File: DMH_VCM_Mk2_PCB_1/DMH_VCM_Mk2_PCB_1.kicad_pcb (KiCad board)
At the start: 2 copper layers, 48 x 175 mm, 95 parts, among them J1 TS_Jack_6.35mm_Sw, J10 TS_Jack_6.35mm_Sw, J100 IDC_02x05, J2 TS_Jack_6.35mm_Sw, J200 IDC_02x05, J3 TS_Jack_6.35mm_Sw, J4 TS_Jack_6.35mm_Sw, J5 TS_Jack_6.35mm_Sw, J50 Conn_01x08, J6 TS_Jack_6.35mm_Sw, J60 Conn_01x08, J7 TS_Jack_6.35mm_Sw, J70 Conn_01x08, J8 TS_Jack_6.35mm_Sw, J9 TS_Jack_6.35mm_Sw, Q1 BC548, Q2 BC548, Q3 BC548, Q4 BC548, Q5 BC548, Q6 BC548, U1 TL074, U2 TL074, U3 TL074

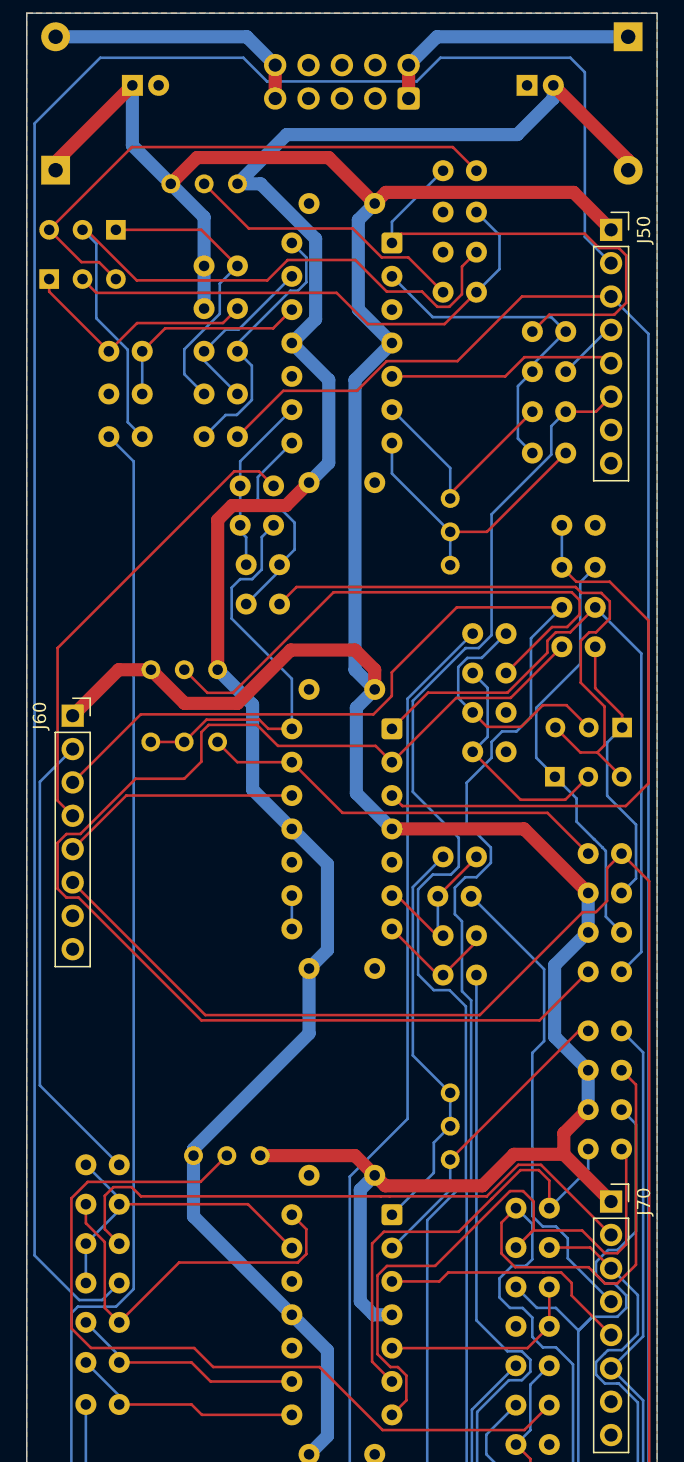
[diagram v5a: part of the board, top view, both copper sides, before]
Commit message: Fixed routing bugs
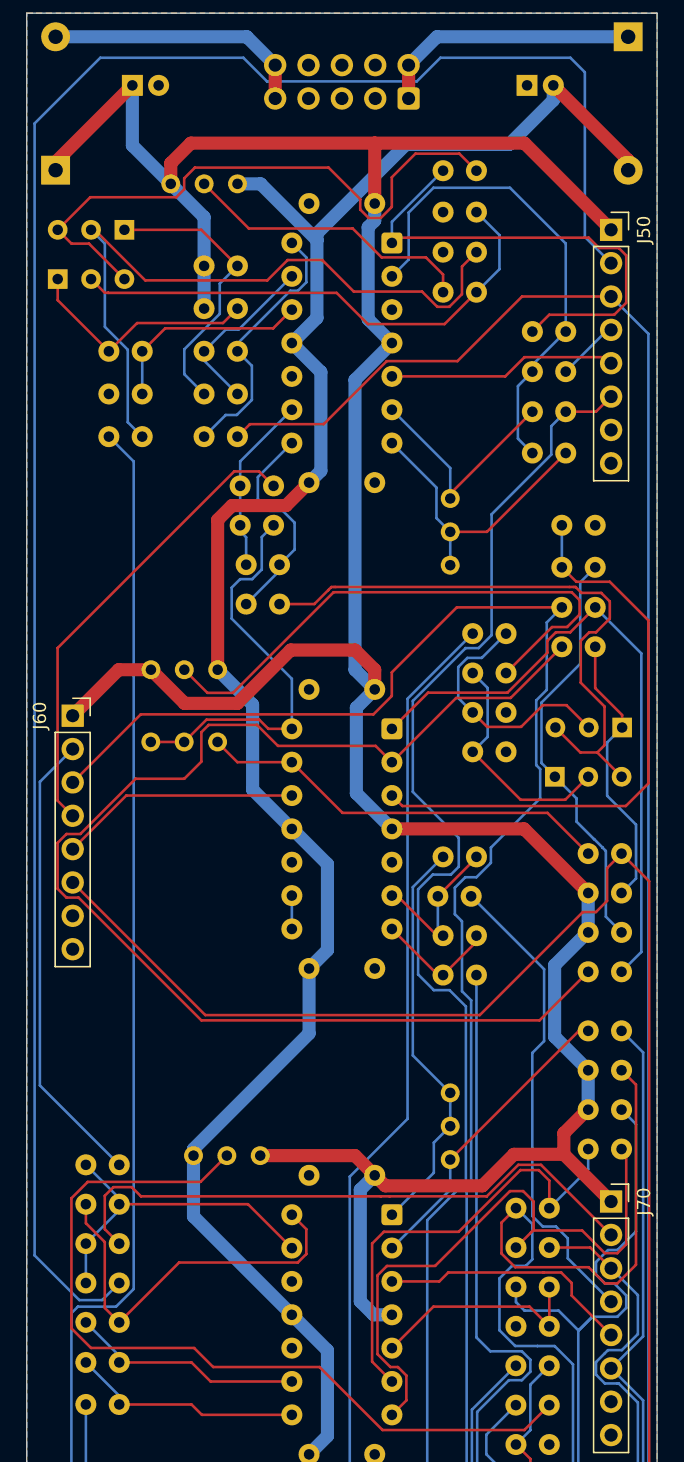
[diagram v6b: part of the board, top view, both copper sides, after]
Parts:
- moved Q1 0.65 mm to (58.4, 59.0)
- moved Q2 0.65 mm to (53.4, 62.8)
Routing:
- net Net-(U1A--): track 26.2 -> 37.8 mm
- net +12V: track 230.3 -> 235.5 mm
- net Net-(Q1-E): track 42.5 -> 46.9 mm
- net -12V: track 157.2 -> 152.8 mm
- net /Inputs and Outputs/Output B Jack: track 151.2 -> 149.3 mm
- net Net-(U3B-+): track 15.7 -> 16.9 mm
- net Net-(Q1-B): track 54.3 -> 53.4 mm
- net Net-(R9-Pad1): track 21.6 -> 22.4 mm
- net Net-(Q5-E): track 57.7 -> 58.5 mm
- net Net-(Q6-C): track 60.4 -> 61.1 mm
- net Net-(Q2-B): track 40.0 -> 39.3 mm
- net Net-(Q1-C): track 22.4 -> 21.8 mm
- net Net-(Q5-C): track 64.5 -> 65.1 mm

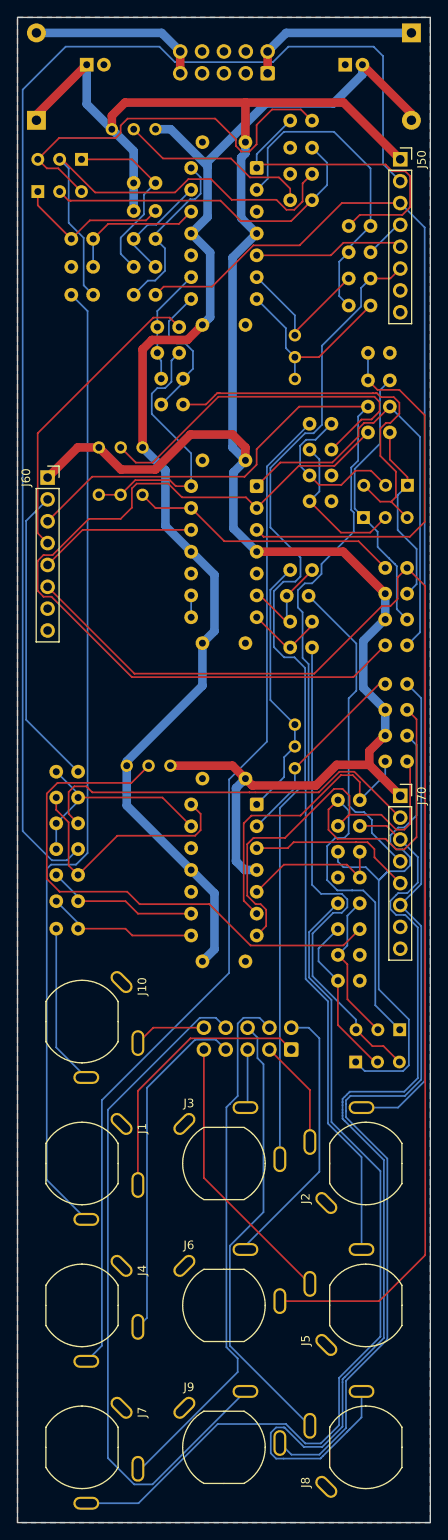
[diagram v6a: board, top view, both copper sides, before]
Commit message: Optimized PCB 1 routing
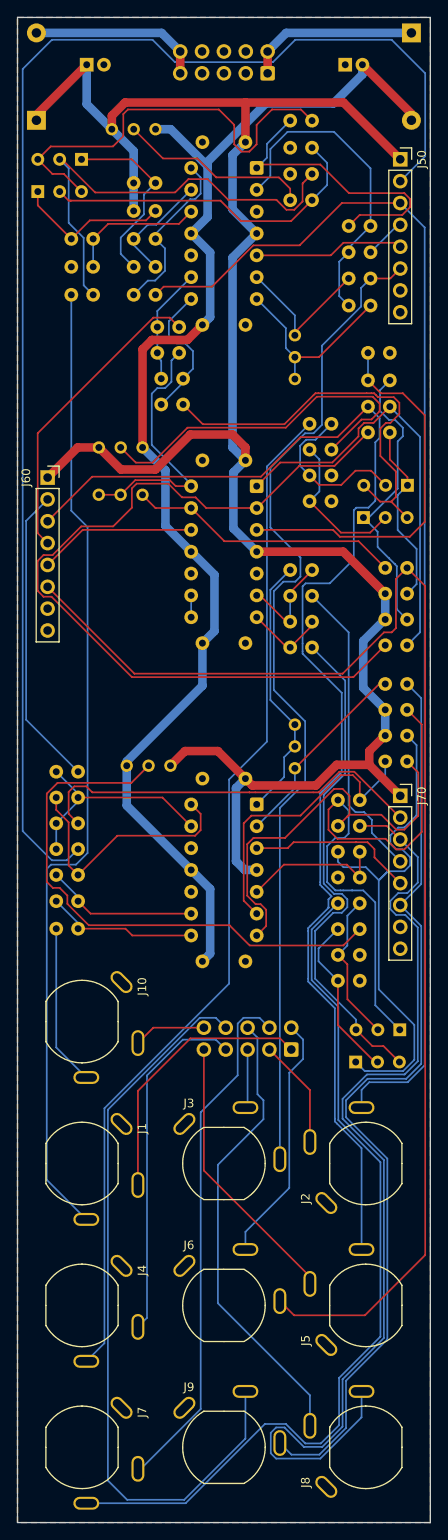
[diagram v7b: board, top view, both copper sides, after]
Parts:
- moved R45 0.40 mm to (85.2, 109.8)
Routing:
- net /Inputs and Outputs/Mute A Switch: track 155.9 -> 162.7 mm
- net Net-(J200-Pin_9): track 80.8 -> 87.1 mm
- net /Inputs and Outputs/Output B Jack: track 149.3 -> 154.7 mm
- net /Inputs and Outputs/CV B Jack: track 152.4 -> 155.7 mm
- net Net-(J200-Pin_6): track 31.9 -> 29.1 mm
- net Net-(Q1-E): track 46.9 -> 49.7 mm
- net +12V: track 235.5 -> 237.7 mm
- net Net-(Q4-C): track 32.0 -> 34.2 mm
- net Net-(Q3-E): track 46.4 -> 48.3 mm
- net Net-(R12-Pad1): track 37.3 -> 35.8 mm
- net Net-(J200-Pin_8): track 52.5 -> 53.7 mm
- net /Inputs and Outputs/Output C Jack: track 118.4 -> 117.2 mm
- net Net-(J200-Pin_7): track 62.3 -> 61.2 mm
- net /Inputs and Outputs/CV C Jack: track 110.1 -> 109.0 mm
- net Net-(Q5-E): track 58.5 -> 59.5 mm
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
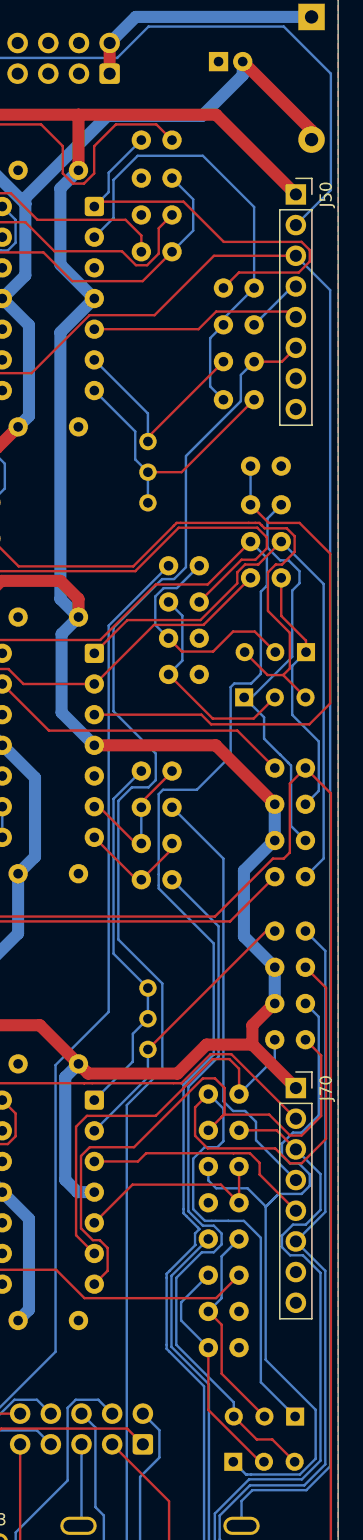
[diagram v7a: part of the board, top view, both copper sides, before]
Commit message: Resolved J50 volume conflict
J70 still to be solved
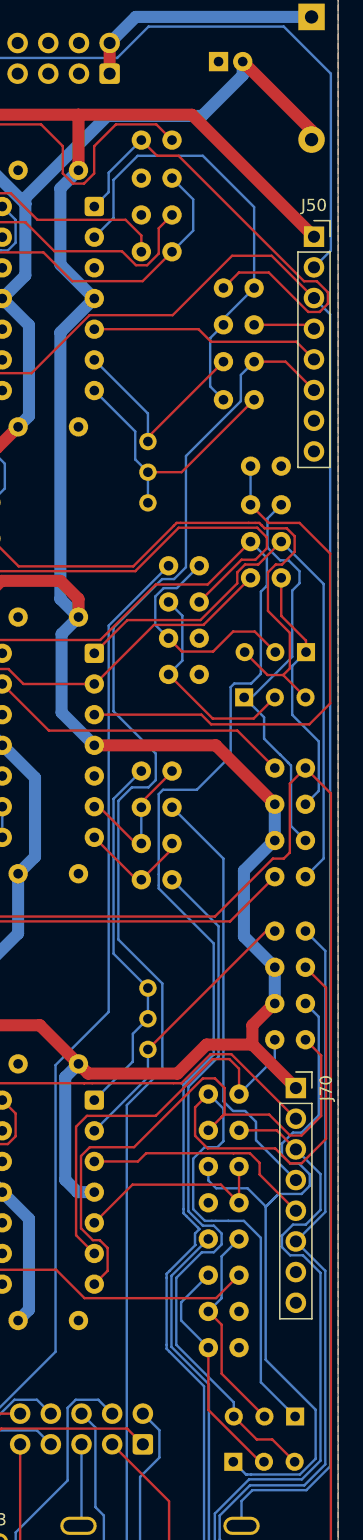
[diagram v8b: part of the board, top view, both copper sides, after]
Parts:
- moved J50 3.81 mm to (97.0, 62.5)
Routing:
- net Net-(R12-Pad1): track 35.8 -> 39.5 mm
- net +12V: track 237.7 -> 240.6 mm
- net /Inputs and Outputs/Mute A Switch: track 162.7 -> 165.6 mm
- net /Inputs and Outputs/CV A Jack: track 118.0 -> 120.0 mm
- net /Inputs and Outputs/CV Amt A Pot: track 17.5 -> 19.2 mm
- net /Inputs and Outputs/Output A Jack: track 144.9 -> 143.7 mm
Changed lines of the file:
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@@
 		(locked yes)
 		(layer "F.Cu")
-		(at 95.5 59)
+		(at 97 62.5)
 		(descr "Through hole straight socket strip, 1x08, 2.54mm pitch, single row (from Kicad 4.0.7), script generated")
 		(tags "Through hole socket strip THT 1x08 2.54mm single row")
 		(property "Reference" "J50"
-			(at 2.5 0 90)
+			(at 0 -2.6 180)
 			(layer "F.SilkS")
 			(effects
@@
 		(tags "Resistor Axial_DIN0207 series Axial Vertical pin pitch 2.54mm 0.25W = 1/4W length 6.3mm diameter 2.5mm")
 		(property "Reference" "R22"
-			(at 5.11 -0.1 0)
+			(at 1.35 -2.1 0)
 			(layer "B.SilkS")
 			(effects
@@
 	)
 	(segment
+		(start 86.9 52.4)
+		(end 97 62.5)
+		(width 1)
+		(layer "F.Cu")
+		(net 1)
+	)
+	(segment
 		(start 78.81 104.62)
 		(end 88.875 104.62)
@@
 	)
 	(segment
-		(start 88.9 52.4)
-		(end 95.5 59)
-		(width 1)
-		(layer "F.Cu")
-		(net 1)
-	)
-	(segment
 		(start 76 91)
 		(end 77.5 92.5)
@@
 	)
 	(segment
-		(start 77.5 52.4)
-		(end 88.9 52.4)
-		(width 1)
-		(layer "F.Cu")
-		(net 1)
-	)
-	(segment
 		(start 63.5 52.4)
 		(end 77.5 52.4)
@@
 	)
 	(segment
+		(start 77.5 52.4)
+		(end 86.9 52.4)
+		(width 1)
+		(layer "F.Cu")
+		(net 1)
+	)
+	(segment
 		(start 76.1 95.4)
 		(end 76.1 101.91)
@@
 	)
 	(segment
+		(start 93.5 64.08)
+		(end 97 67.58)
+		(width 0.2)
+		(layer "F.Cu")
+		(net 9)
+	)
+	(segment
 		(start 67.045 74.75)
 		(end 67.995 73.8)
@@
 	)
 	(segment
-		(start 83.8 69)
-		(end 88.72 64.08)
+		(start 85.3 69)
+		(end 90.22 64.08)
 		(width 0.2)
 		(layer "F.Cu")
@@
 	)
 	(segment
-		(start 88.72 64.08)
-		(end 95.5 64.08)
+		(start 90.22 64.08)
+		(end 93.5 64.08)
 		(width 0.2)
 		(layer "F.Cu")
@@
 	(segment
 		(start 78.41295 69)
-		(end 83.8 69)
+		(end 85.3 69)
 		(width 0.2)
 		(layer "F.Cu")
@@
 	)
 	(segment
-		(start 96.3661 166.301)
-		(end 91.899 166.301)
+		(start 98.341 68.921)
+		(end 98.341 164.3261)
 		(width 0.2)
 		(layer "B.Cu")
@@
 	)
 	(segment
-		(start 95.5 64.08)
-		(end 98.341 66.921)
+		(start 96.3661 166.301)
+		(end 91.899 166.301)
 		(width 0.2)
 		(layer "B.Cu")
@@
 	)
 	(segment
-		(start 91.899 166.301)
-		(end 91 167.2)
+		(start 97 67.58)
+		(end 98.341 68.921)
 		(width 0.2)
 		(layer "B.Cu")
@@
 	)
 	(segment
-		(start 91 167.2)
-		(end 91 169.25)
+		(start 98.341 164.3261)
+		(end 96.3661 166.301)
 		(width 0.2)
 		(layer "B.Cu")
@@
 	)
 	(segment
-		(start 98.341 66.921)
-		(end 98.341 164.3261)
+		(start 91.899 166.301)
+		(end 91 167.2)
 		(width 0.2)
 		(layer "B.Cu")
@@
 	)
 	(segment
-		(start 98.341 164.3261)
-		(end 96.3661 166.301)
+		(start 91 167.2)
+		(end 91 169.25)
 		(width 0.2)
 		(layer "B.Cu")
@@
 	)
 	(segment
-		(start 92.045 72.85)
-		(end 94.35 72.85)
+		(start 94.65 72.85)
+		(end 97 75.2)
 		(width 0.2)
 		(layer "F.Cu")
@@
 	)
 	(segment
-		(start 94.35 72.85)
-		(end 95.5 71.7)
+		(start 92.045 72.85)
+		(end 94.65 72.85)
 		(width 0.2)
 		(layer "F.Cu")
@@
 	)
 	(segment
-		(start 95.225 66.62)
-		(end 95.5 66.62)
+		(start 92.045 69.8)
+		(end 96.68 69.8)
 		(width 0.2)
-		(layer "B.Cu")
+		(layer "F.Cu")
 		(net 26)
 	)
 	(segment
-		(start 92.045 69.8)
-		(end 95.225 66.62)
+		(start 96.68 69.8)
+		(end 97 70.12)
 		(width 0.2)
-		(layer "B.Cu")
+		(layer "F.Cu")
 		(net 26)
 	)
 	(segment
-		(start 66.701 45.101)
-		(end 69.3 47.7)
+		(start 58.045 139.2)
+		(end 56.745 140.5)
 		(width 0.2)
 		(layer "B.Cu")
@@
 	(segment
 		(start 98.399 48.999)
-		(end 98.399 58.641)
-		(width 0.2)
-		(layer "B.Cu")
-		(net 27)
-	)
-	(segment
-		(start 51.601 137.101)
-		(end 51.601 48.499)
+		(end 98.399 63.641)
 		(width 0.2)
 		(layer "B.Cu")
@@
 	)
 	(segment
-		(start 55 140.5)
-		(end 51.601 137.101)
+		(start 56.745 140.5)
+		(end 55 140.5)
 		(width 0.2)
 		(layer "B.Cu")
@@
 	)
 	(segment
-		(start 69.3 47.7)
-		(end 80.7 47.7)
+		(start 55 140.5)
+		(end 51.601 137.101)
 		(width 0.2)
 		(layer "B.Cu")
@@
 	)
 	(segment
-		(start 56.745 140.5)
-		(end 55 140.5)
+		(start 94.501 45.101)
+		(end 98.399 48.999)
 		(width 0.2)
 		(layer "B.Cu")
@@
 	)
 	(segment
-		(start 94.501 45.101)
-		(end 98.399 48.999)
+		(start 51.601 137.101)
+		(end 51.601 48.499)
 		(width 0.2)
 		(layer "B.Cu")
@@
 	)
 	(segment
-		(start 98.399 58.641)
-		(end 95.5 61.54)
+		(start 98.399 63.641)
+		(end 97 65.04)
 		(width 0.2)
 		(layer "B.Cu")
@@
 	)
 	(segment
-		(start 58.045 139.2)
-		(end 56.745 140.5)
+		(start 69.3 47.7)
+		(end 80.7 47.7)
 		(width 0.2)
 		(layer "B.Cu")
@@
 	)
 	(segment
-		(start 83.299 45.101)
-		(end 94.501 45.101)
+		(start 66.701 45.101)
+		(end 69.3 47.7)
 		(width 0.2)
 		(layer "B.Cu")
@@
 	)
 	(segment
+		(start 83.299 45.101)
+		(end 94.501 45.101)
+		(width 0.2)
+		(layer "B.Cu")
+		(net 27)
+	)
+	(segment
 		(start 52.002 101.038)
 		(end 52.002 124.157)
@@
 	)
 	(segment
-		(start 78.81 60)
-		(end 79.21 59.6)
+		(start 97.47676 68.731)
+		(end 98.151 68.05676)
+		(width 0.2)
+		(layer "F.Cu")
+		(net 50)
+	)
+	(segment
+		(start 85.7871 55.8)
+		(end 84.005 55.8)
+		(width 0.2)
+		(layer "F.Cu")
+		(net 50)
+	)
+	(segment
+		(start 97.23876 66.191)
+		(end 96.1781 66.191)
 		(width 0.2)
 		(layer "F.Cu")
@@
 	)
 	(segment
-		(start 79.21 59.6)
-		(end 86.2 59.6)
+		(start 98.151 68.05676)
+		(end 98.151 67.10324)
 		(width 0.2)
 		(layer "F.Cu")
@@
 	)
 	(segment
-		(start 95.73876 65.469)
+		(start 89.505 66.75)
 		(end 90.786 65.469)
 		(width 0.2)
@@
 	)
 	(segment
-		(start 89.529 62.929)
-		(end 95.97676 62.929)
+		(start 93.26124 65.469)
+		(end 96.52324 68.731)
 		(width 0.2)
 		(layer "F.Cu")
@@
 	)
 	(segment
-		(start 90.786 65.469)
-		(end 89.505 66.75)
+		(start 98.151 67.10324)
+		(end 97.23876 66.191)
 		(width 0.2)
 		(layer "F.Cu")
@@
 	)
 	(segment
-		(start 86.2 59.6)
-		(end 89.529 62.929)
+		(start 96.52324 68.731)
+		(end 97.47676 68.731)
 		(width 0.2)
 		(layer "F.Cu")
@@
 	)
 	(segment
-		(start 95.97676 62.929)
-		(end 96.651 63.60324)
+		(start 90.786 65.469)
+		(end 93.26124 65.469)
 		(width 0.2)
 		(layer "F.Cu")
@@
 	)
 	(segment
-		(start 96.651 64.55676)
-		(end 95.73876 65.469)
+		(start 96.1781 66.191)
+		(end 85.7871 55.8)
 		(width 0.2)
 		(layer "F.Cu")
@@
 	)
 	(segment
-		(start 96.651 63.60324)
-		(end 96.651 64.55676)
+		(start 84.005 55.8)
+		(end 82.705 54.5)
 		(width 0.2)
 		(layer "F.Cu")
@@
 	)
 	(segment
-		(start 88.901 68.699)
-		(end 95.039 68.699)
+		(start 88.48 71.2)
+		(end 95.54 71.2)
 		(width 0.2)
 		(layer "F.Cu")
@@
 	)
 	(segment
-		(start 95.039 68.699)
-		(end 95.5 69.16)
+		(start 78.81 70.16)
+		(end 87.44 70.16)
 		(width 0.2)
 		(layer "F.Cu")
@@
 	(segment
 		(start 87.44 70.16)
-		(end 88.901 68.699)
+		(end 88.48 71.2)
 		(width 0.2)
 		(layer "F.Cu")
@@
 	)
 	(segment
-		(start 78.81 70.16)
-		(end 87.44 70.16)
+		(start 95.54 71.2)
+		(end 97 72.66)
 		(width 0.2)
 		(layer "F.Cu")
